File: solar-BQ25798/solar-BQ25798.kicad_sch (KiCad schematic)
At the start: 72 parts, among them J101 Power In, J102 Power OUT, J103 Power OUT

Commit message: BQ25798 WIP
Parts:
- removed BAT_N116: MY-18650-05-J, cacophony-library:BAT-TH_MY-18650-05-J, symbol cacophony-library:MY-18650-05-J
- removed BAT_P116: MY-18650-04-J, cacophony-library:BAT-TH_MY-18650-04-J, symbol cacophony-library:MY-18650-04-J
- added D101: D_Zener, Diode_SMD:D_SOD-123, symbol Device:D_Zener
- added Q101: DMP4013LFGQ-13, Package_SON:Diodes_PowerDI3333-8, symbol cacophony-library:DMP4013LFGQ-13
- added R102: 100k, Resistor_SMD:R_0402_1005Metric, symbol Device:R
- F101, F102: value Fuse -> 8A; footprint Fuse:Fuse_0805_2012Metric -> Fuse:Fuse_1206_3216Metric; LCSC Part (none) -> C187562
- R101: value 1k -> 10k; footprint Resistor_SMD:R_0603_1608Metric -> Resistor_SMD:R_0402_1005Metric; LCSC Part (none) -> C25744
- renumbered FL102 to FL101, FL103 to FL102, H105 to H102, H109 to H103, H102 to H104, H106 to H105, H110 to H106, H103 to H107, H107 to H108, H111 to H109, H104 to H110, H108 to H111, H117 to H114, H121 to H115, H114 to H116, H118 to H117, H122 to H118, H115 to H119, H119 to H120, H123 to H121, H116 to H122, H120 to H123, H129 to H126, H126 to H127, H130 to H128, H127 to H129, H131 to H130, H128 to H131, J103 to J102, J102 to J103
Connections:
- net GND: now also R102.1; no longer FL102.2
- net GND_OUT_FILTERED: now also J102.2 (Pin_2), J103.2 (Pin_2); no longer J102.1 (Pin_1), J103.1 (Pin_1)
- net POWER_IN_FILTERED: now also FL101.3, Q101.5 (D); no longer F101.2, FL101.2
- net V_BATT_FUSED: now also J102.1 (Pin_1), J103.1 (Pin_1); no longer J102.2 (Pin_2), J103.2 (Pin_2)
- net V_{IN}: now also D101.1 (K), Q101.1 (S), Q101.2 (S), Q101.3 (S); no longer FL101.3
- net GND_IN_FILTERED renamed GND_IN_PHY
- net V_BATT renamed PACK_+
- net cell_S1_1/BAT+ renamed cell_S1_1/CELL+
- net cell_S1_1/BAT- renamed cell_S1_1/CELL-
- net cell_10/BAT+ renamed cell_S1_10/CELL+
- net cell_10/BAT- renamed cell_S1_10/CELL-
- net cell_11/BAT+ renamed cell_S1_11/CELL+
- net cell_11/BAT- renamed cell_S1_11/CELL-
- net cell_12/BAT+ renamed cell_S1_12/CELL+
- net cell_12/BAT- renamed cell_S1_12/CELL-
- net cell_13/BAT+ renamed cell_S1_13/CELL+
- net cell_13/BAT- renamed cell_S1_13/CELL-
- net cell_14/BAT+ renamed cell_S1_14/CELL+
- net cell_14/BAT- renamed cell_S1_14/CELL-
- net cell_15/BAT+ renamed cell_S1_15/CELL+
- net cell_15/BAT- renamed cell_S1_15/CELL-
- net cell_2/BAT+ renamed cell_S1_2/CELL+
- net cell_2/BAT- renamed cell_S1_2/CELL-
- net cell_3/BAT+ renamed cell_S1_3/CELL+
- net cell_3/BAT- renamed cell_S1_3/CELL-
- net cell_4/BAT+ renamed cell_S1_4/CELL+
- net cell_4/BAT- renamed cell_S1_4/CELL-
- net cell_5/BAT+ renamed cell_S1_5/CELL+
- net cell_5/BAT- renamed cell_S1_5/CELL-
- net cell_6/BAT+ renamed cell_S1_6/CELL+
- net cell_6/BAT- renamed cell_S1_6/CELL-
- net cell_7/BAT+ renamed cell_S1_7/CELL+
- net cell_7/BAT- renamed cell_S1_7/CELL-
- net cell_8/BAT+ renamed cell_S1_8/CELL+
- net cell_8/BAT- renamed cell_S1_8/CELL-
- net cell_9/BAT+ renamed cell_S1_9/CELL+
- net cell_9/BAT- renamed cell_S1_9/CELL-
- new net: D101.2 (A), Q101.4 (G), R102.2
- new net PACK_-: FL102.2
- new net POWER_IN_FUSED: F101.2, FL101.2
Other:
- sheet cell_1 renamed cell_S1_1
- removed sheet LTC4015 Sheet
- removed sheet cell_10
- removed sheet cell_11
- removed sheet cell_12
- removed sheet cell_13
- removed sheet cell_14
- removed sheet cell_15
- removed sheet cell_16
- removed sheet cell_2
- removed sheet cell_3
- removed sheet cell_4
- removed sheet cell_5
- removed sheet cell_6
- removed sheet cell_7
- removed sheet cell_8
- removed sheet cell_9
- added sheet ATtiny1616 (attiny1616.kicad_sch)
- added sheet BQ25798 (BQ25798.kicad_sch)
- added sheet BQ76920 (bq76920.kicad_sch)
- added sheet cell_S1_10 (cell_S1_1.kicad_sch)
- added sheet cell_S1_11 (cell_S1_1.kicad_sch)
- added sheet cell_S1_12 (cell_S1_1.kicad_sch)
- added sheet cell_S1_13 (cell_S1_1.kicad_sch)
- added sheet cell_S1_14 (cell_S1_1.kicad_sch)
- added sheet cell_S1_15 (cell_S1_1.kicad_sch)
- added sheet cell_S1_2 (cell_S1_1.kicad_sch)
- added sheet cell_S1_3 (cell_S1_1.kicad_sch)
- added sheet cell_S1_4 (cell_S1_1.kicad_sch)
- added sheet cell_S1_5 (cell_S1_1.kicad_sch)
- added sheet cell_S1_6 (cell_S1_1.kicad_sch)
- added sheet cell_S1_7 (cell_S1_1.kicad_sch)
- added sheet cell_S1_8 (cell_S1_1.kicad_sch)
- added sheet cell_S1_9 (cell_S1_1.kicad_sch)
- sheet cell_S1_1: file cell_1.kicad_sch -> cell_S1_1.kicad_sch
- sheet cell_S1_1 ports: added CELL+, CELL-, CELL_PROTECTED+, CELL_PROTECTED-; removed BAT+, BAT-
- moved on the sheet: BAT_N101, BAT_P101, F101, F102, FL101, FL102, H101, H102, H103, H104, H105, H106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

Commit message: BQ25798 WIP
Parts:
- F101, F102: value 8A -> 4A; footprint Fuse:Fuse_1206_3216Metric -> cacophony-library:FUSE-SMD_2410F4A250V; LCSC Part C187562 -> C5220740
- renumbered BAT_N106 to BAT_N102, BAT_N111 to BAT_N103, BAT_N102 to BAT_N104, BAT_N107 to BAT_N105, BAT_N112 to BAT_N106, BAT_N103 to BAT_N107, BAT_N113 to BAT_N109, BAT_N104 to BAT_N110, BAT_N109 to BAT_N111, BAT_N114 to BAT_N112, BAT_N105 to BAT_N113, BAT_N110 to BAT_N114, BAT_P106 to BAT_P102, BAT_P111 to BAT_P103, BAT_P102 to BAT_P104, BAT_P107 to BAT_P105, BAT_P112 to BAT_P106, BAT_P103 to BAT_P107, BAT_P113 to BAT_P109, BAT_P104 to BAT_P110, BAT_P109 to BAT_P111, BAT_P114 to BAT_P112, BAT_P105 to BAT_P113, BAT_P110 to BAT_P114, H104 to H102, H107 to H103, H110 to H104, H113 to H105, H116 to H106, H119 to H107, H122 to H108, H125 to H109, H127 to H110, H129 to H111, H131 to H112, H102 to H113, H105 to H114, H108 to H115, H111 to H116, H114 to H117, H117 to H118, H120 to H119, H123 to H120, H126 to H121, H128 to H122, H130 to H123, H132 to H124, H103 to H125, H106 to H126, H109 to H127, H112 to H128, H115 to H129, H118 to H130, H121 to H131, H124 to H132
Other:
- sheet cell_S1_1 renamed cell_01
- sheet cell_S1_10 renamed cell_10
- sheet cell_S1_11 renamed cell_11
- sheet cell_S1_12 renamed cell_12
- sheet cell_S1_13 renamed cell_13
- sheet cell_S1_14 renamed cell_14
- sheet cell_S1_15 renamed cell_15
- sheet cell_S1_2 renamed cell_02
- sheet cell_S1_3 renamed cell_03
- sheet cell_S1_4 renamed cell_04
- sheet cell_S1_5 renamed cell_05
- sheet cell_S1_6 renamed cell_06
- sheet cell_S1_7 renamed cell_07
- sheet cell_S1_8 renamed cell_08
- sheet cell_S1_9 renamed cell_09
- sheet BQ76920: file bq76920.kicad_sch -> BQ76920.kicad_sch
- sheet cell_01: file cell_S1_1.kicad_sch -> cell.kicad_sch
- sheet cell_02: file cell_S1_1.kicad_sch -> cell.kicad_sch
- sheet cell_03: file cell_S1_1.kicad_sch -> cell.kicad_sch
- sheet cell_04: file cell_S1_1.kicad_sch -> cell.kicad_sch
- sheet cell_05: file cell_S1_1.kicad_sch -> cell.kicad_sch
- sheet cell_06: file cell_S1_1.kicad_sch -> cell.kicad_sch
- sheet cell_07: file cell_S1_1.kicad_sch -> cell.kicad_sch
- sheet cell_08: file cell_S1_1.kicad_sch -> cell.kicad_sch
- sheet cell_09: file cell_S1_1.kicad_sch -> cell.kicad_sch
- sheet cell_10: file cell_S1_1.kicad_sch -> cell.kicad_sch
- sheet cell_11: file cell_S1_1.kicad_sch -> cell.kicad_sch
- sheet cell_12: file cell_S1_1.kicad_sch -> cell.kicad_sch
- sheet cell_13: file cell_S1_1.kicad_sch -> cell.kicad_sch
- sheet cell_14: file cell_S1_1.kicad_sch -> cell.kicad_sch
- sheet cell_15: file cell_S1_1.kicad_sch -> cell.kicad_sch
- note removed: "C2915633"
- moved on the sheet: BAT_N101, BAT_N102, BAT_N103, BAT_N104, BAT_N105, BAT_N106, BAT_N107, BAT_N108, BAT_N109, BAT_N110, BAT_N111, BAT_N112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

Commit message: Solar battery WIP
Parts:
- added C101, C102: 1uF, Capacitor_SMD:C_0603_1608Metric, symbol Device:C_Small
- added D102, D103: D, Diode_SMD:D_SOD-323_HandSoldering, symbol Device:D
- added JP101: Jumper_2_Open, Connector_PinHeader_2.00mm:PinHeader_2x01_P2.00mm_Vertical, symbol Jumper:Jumper_2_Open
- added JP102: SolderJumper_2_Bridged, cacophony-library:SolderJumper-2_P1.3mm_Bridged_RoundedPad1.0x1.5mm, symbol Jumper:SolderJumper_2_Bridged
- added Q102: 2N7002, Package_TO_SOT_SMD:SOT-23, symbol Transistor_FET:2N7002
- added R103: 30k, Resistor_SMD:R_0402_1005Metric, symbol Device:R
- added R104: 10k, Resistor_SMD:R_0402_1005Metric, symbol Device:R
- added U101: HT75xx-1-SOT89, Package_TO_SOT_SMD:SOT-89-3, symbol Regulator_Linear:HT75xx-1-SOT89
- BAT_N101, BAT_N108, BAT_N115: footprint cacophony-library:BAT-TH_MY-18650-05-J -> cacophony-library:BAT-TH_MY-18650-05-J-2
- BAT_N102: renamed from BAT_N104; footprint cacophony-library:BAT-TH_MY-18650-05-J -> cacophony-library:BAT-TH_MY-18650-05-J-2
- BAT_N103: renamed from BAT_N107; footprint cacophony-library:BAT-TH_MY-18650-05-J -> cacophony-library:BAT-TH_MY-18650-05-J-2
- BAT_N104: renamed from BAT_N110; footprint cacophony-library:BAT-TH_MY-18650-05-J -> cacophony-library:BAT-TH_MY-18650-05-J-2
- BAT_N105: renamed from BAT_N113; footprint cacophony-library:BAT-TH_MY-18650-05-J -> cacophony-library:BAT-TH_MY-18650-05-J-2
- BAT_N106: renamed from BAT_N102; footprint cacophony-library:BAT-TH_MY-18650-05-J -> cacophony-library:BAT-TH_MY-18650-05-J-2
- BAT_N107: renamed from BAT_N105; footprint cacophony-library:BAT-TH_MY-18650-05-J -> cacophony-library:BAT-TH_MY-18650-05-J-2
- BAT_N109: renamed from BAT_N111; footprint cacophony-library:BAT-TH_MY-18650-05-J -> cacophony-library:BAT-TH_MY-18650-05-J-2
- BAT_N110: renamed from BAT_N114; footprint cacophony-library:BAT-TH_MY-18650-05-J -> cacophony-library:BAT-TH_MY-18650-05-J-2
- BAT_N111: renamed from BAT_N103; footprint cacophony-library:BAT-TH_MY-18650-05-J -> cacophony-library:BAT-TH_MY-18650-05-J-2
- BAT_N112: renamed from BAT_N106; footprint cacophony-library:BAT-TH_MY-18650-05-J -> cacophony-library:BAT-TH_MY-18650-05-J-2
- BAT_N113: renamed from BAT_N109; footprint cacophony-library:BAT-TH_MY-18650-05-J -> cacophony-library:BAT-TH_MY-18650-05-J-2
- BAT_N114: renamed from BAT_N112; footprint cacophony-library:BAT-TH_MY-18650-05-J -> cacophony-library:BAT-TH_MY-18650-05-J-2
- BAT_P101, BAT_P108, BAT_P115: footprint cacophony-library:BAT-TH_MY-18650-04-J -> cacophony-library:BAT-TH_MY-18650-test8_4.0_2.5
- BAT_P102: renamed from BAT_P104; footprint cacophony-library:BAT-TH_MY-18650-04-J -> cacophony-library:BAT-TH_MY-18650-test8_4.0_2.5
- BAT_P103: renamed from BAT_P107; footprint cacophony-library:BAT-TH_MY-18650-04-J -> cacophony-library:BAT-TH_MY-18650-test8_4.0_2.5
- BAT_P104: renamed from BAT_P110; footprint cacophony-library:BAT-TH_MY-18650-04-J -> cacophony-library:BAT-TH_MY-18650-test8_4.0_2.5
- BAT_P105: renamed from BAT_P113; footprint cacophony-library:BAT-TH_MY-18650-04-J -> cacophony-library:BAT-TH_MY-18650-test8_4.0_2.5
- BAT_P106: renamed from BAT_P102; footprint cacophony-library:BAT-TH_MY-18650-04-J -> cacophony-library:BAT-TH_MY-18650-test8_4.0_2.5
- BAT_P107: renamed from BAT_P105; footprint cacophony-library:BAT-TH_MY-18650-04-J -> cacophony-library:BAT-TH_MY-18650-test8_4.0_2.5
- BAT_P109: renamed from BAT_P111; footprint cacophony-library:BAT-TH_MY-18650-04-J -> cacophony-library:BAT-TH_MY-18650-test8_4.0_2.5
- BAT_P110: renamed from BAT_P114; footprint cacophony-library:BAT-TH_MY-18650-04-J -> cacophony-library:BAT-TH_MY-18650-test8_4.0_2.5
- BAT_P111: renamed from BAT_P103; footprint cacophony-library:BAT-TH_MY-18650-04-J -> cacophony-library:BAT-TH_MY-18650-test8_4.0_2.5
- BAT_P112: renamed from BAT_P106; footprint cacophony-library:BAT-TH_MY-18650-04-J -> cacophony-library:BAT-TH_MY-18650-test8_4.0_2.5
- BAT_P113: renamed from BAT_P109; footprint cacophony-library:BAT-TH_MY-18650-04-J -> cacophony-library:BAT-TH_MY-18650-test8_4.0_2.5
- BAT_P114: renamed from BAT_P112; footprint cacophony-library:BAT-TH_MY-18650-04-J -> cacophony-library:BAT-TH_MY-18650-test8_4.0_2.5
- renumbered F102 to F101, F101 to F102, FL102 to FL101, FL101 to FL102, H113 to H102, H125 to H103, H109 to H104, H102 to H105, H114 to H106, H126 to H107, H110 to H108, H103 to H109, H115 to H110, H127 to H111, H111 to H112, H104 to H113, H116 to H114, H128 to H115, H121 to H116, H105 to H117, H117 to H118, H129 to H119, H122 to H120, H106 to H121, H118 to H122, H130 to H123, H123 to H124, H107 to H125, H119 to H126, H131 to H127, H112 to H128, H108 to H129, H120 to H130, H132 to H131, H124 to H132, J103 to J101, J101 to J102, J102 to J103
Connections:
- net GND: now also FL102.3, C101.1, C102.1, Q102.2 (S), R104.2, U101.1 (GND); no longer FL102.4
- net GND_IN_PHY: now also FL102.2; no longer FL102.1
- net PACK_+: now also D102.2 (A), JP101.2 (B), JP102.2 (B)
- net POWER_IN_FILTERED: now also FL102.4; no longer FL102.3
- net POWER_IN_FUSED: now also FL102.1; no longer FL102.2
- net V_{IN}: now also D103.2 (A)
- net V_{SENSE}: now also Q102.3 (D), R103.1
- new net +3.3V: C102.2, U101.3 (VOUT)
- new net PACK_+_PHY: JP101.1 (A), JP102.1 (A)
- new net PRE_LIN_REG: C101.2, D102.1 (K), D103.1 (K), U101.2 (VIN)
- new net PULL_SENSE_LOW: Q102.1 (G)
- new net SENSE_DIV: R103.2, R104.1
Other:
- note added: "3.3V Power supply"
- note added: "Mounting Holes"
- note added: "Power In"
- note added: "Power OUT"
- moved on the sheet: BAT_N101, BAT_N102, BAT_N103, BAT_N104, BAT_N105, BAT_N106, BAT_N107, BAT_N108, BAT_N109, BAT_N110, BAT_N111, BAT_N112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

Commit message: Version v0.0.2
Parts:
- JP101: now left out of the parts list
- Q102: LCSC Part (none) -> C8545
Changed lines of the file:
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@@
 		(unit 1)
 		(exclude_from_sim no)
-		(in_bom yes)
+		(in_bom no)
 		(on_board yes)
 		(dnp no)
@@
 			(at 144.78 55.88 0)
 			(effects
+				(font
+					(size 1.27 1.27)
+				)
+				(hide yes)
+			)
+		)
+		(property "LCSC Part" "C8545"
+			(at 144.78 55.88 0)
+			(effects

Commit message: Tidy up of files
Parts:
- added C?: 22pF, Capacitor_SMD:C_0402_1005Metric, symbol Device:C_Small
- added Q103: 2N7002, Package_TO_SOT_SMD:SOT-23, symbol Transistor_FET:2N7002
- added R105, R107, R?: 10k, Resistor_SMD:R_0402_1005Metric, symbol Device:R
- added R106: 30k, Resistor_SMD:R_0402_1005Metric, symbol Device:R
- added R108, R?: 1M, Resistor_SMD:R_0603_1608Metric, symbol Device:R
- added R?: 470k, Resistor_SMD:R_0402_1005Metric, symbol Device:R
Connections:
- net GND: now also C?.1, Q103.2 (S), R107.2, R?.2
- net PULL_SENSE_LOW: now also Q103.1 (G)
- net SENSE_DIV: now also R106.2, R107.1
- new net: Q103.3 (D), R105.1, R106.1, R108.1
- new net +12V: R105.2
- new net BATTERY_LV: R108.2, R?.1
- new net BATT_SENSE_LV: C?.2, R?.1, R?.2, R?.2
- new net BATT_SENSE_LV_PHY: R?.1

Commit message: Update battery PCB
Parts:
- removed C?: 22pF, Capacitor_SMD:C_0402_1005Metric, symbol Device:C_Small
- removed H109, H113: MountingHole, cacophony-library:MountingHole_3.2mm_no_bolt_head, symbol Mechanical:MountingHole
- removed JP101: Jumper_2_Open, Connector_PinHeader_2.00mm:PinHeader_2x01_P2.00mm_Vertical, symbol Jumper:Jumper_2_Open
- removed JP102: SolderJumper_2_Bridged, cacophony-library:SolderJumper-2_P1.3mm_Bridged_RoundedPad1.0x1.5mm, symbol Jumper:SolderJumper_2_Bridged
- removed Q103: 2N7002, Package_TO_SOT_SMD:SOT-23, symbol Transistor_FET:2N7002
- removed R105, R107, R?: 10k, Resistor_SMD:R_0402_1005Metric, symbol Device:R
- removed R106: 30k, Resistor_SMD:R_0402_1005Metric, symbol Device:R
- removed R108, R?: 1M, Resistor_SMD:R_0603_1608Metric, symbol Device:R
- removed R?: 470k, Resistor_SMD:R_0402_1005Metric, symbol Device:R
- added C103: 100n, Capacitor_SMD:C_0402_1005Metric, symbol Device:C_Small
- added R107: 0Ω, cacophony-library:R_1206_Shunt, symbol Device:R_Shunt
- added U102: INA219AxDCN, Package_TO_SOT_SMD:SOT-23-8, symbol Sensor_Energy:INA219AxDCN
- BAT_N101, BAT_N108, BAT_N115: footprint cacophony-library:BAT-TH_MY-18650-05-J-2 -> cacophony-library:BAT-TH-18650-N
- BAT_N102: renamed from BAT_N106; footprint cacophony-library:BAT-TH_MY-18650-05-J-2 -> cacophony-library:BAT-TH-18650-N
- BAT_N103: renamed from BAT_N111; footprint cacophony-library:BAT-TH_MY-18650-05-J-2 -> cacophony-library:BAT-TH-18650-N
- BAT_N104: renamed from BAT_N102; footprint cacophony-library:BAT-TH_MY-18650-05-J-2 -> cacophony-library:BAT-TH-18650-N
- BAT_N105: renamed from BAT_N107; footprint cacophony-library:BAT-TH_MY-18650-05-J-2 -> cacophony-library:BAT-TH-18650-N
- BAT_N106: renamed from BAT_N112; footprint cacophony-library:BAT-TH_MY-18650-05-J-2 -> cacophony-library:BAT-TH-18650-N
- BAT_N107: renamed from BAT_N103; footprint cacophony-library:BAT-TH_MY-18650-05-J-2 -> cacophony-library:BAT-TH-18650-N
- BAT_N109: renamed from BAT_N113; footprint cacophony-library:BAT-TH_MY-18650-05-J-2 -> cacophony-library:BAT-TH-18650-N
- BAT_N110: renamed from BAT_N104; footprint cacophony-library:BAT-TH_MY-18650-05-J-2 -> cacophony-library:BAT-TH-18650-N
- BAT_N111: renamed from BAT_N109; footprint cacophony-library:BAT-TH_MY-18650-05-J-2 -> cacophony-library:BAT-TH-18650-N
- BAT_N112: renamed from BAT_N114; footprint cacophony-library:BAT-TH_MY-18650-05-J-2 -> cacophony-library:BAT-TH-18650-N
- BAT_N113: renamed from BAT_N105; footprint cacophony-library:BAT-TH_MY-18650-05-J-2 -> cacophony-library:BAT-TH-18650-N
- BAT_N114: renamed from BAT_N110; footprint cacophony-library:BAT-TH_MY-18650-05-J-2 -> cacophony-library:BAT-TH-18650-N
- BAT_P101, BAT_P108, BAT_P115: footprint cacophony-library:BAT-TH_MY-18650-test8_4.0_2.5 -> cacophony-library:BAT-TH-18650-P_silkscreen
- BAT_P102: renamed from BAT_P106; footprint cacophony-library:BAT-TH_MY-18650-test8_4.0_2.5 -> cacophony-library:BAT-TH-18650-P_silkscreen
- BAT_P103: renamed from BAT_P111; footprint cacophony-library:BAT-TH_MY-18650-test8_4.0_2.5 -> cacophony-library:BAT-TH-18650-P_silkscreen
- BAT_P104: renamed from BAT_P102; footprint cacophony-library:BAT-TH_MY-18650-test8_4.0_2.5 -> cacophony-library:BAT-TH-18650-P_silkscreen
- BAT_P105: renamed from BAT_P107; footprint cacophony-library:BAT-TH_MY-18650-test8_4.0_2.5 -> cacophony-library:BAT-TH-18650-P_silkscreen
- BAT_P106: renamed from BAT_P112; footprint cacophony-library:BAT-TH_MY-18650-test8_4.0_2.5 -> cacophony-library:BAT-TH-18650-P_silkscreen
- BAT_P107: renamed from BAT_P103; footprint cacophony-library:BAT-TH_MY-18650-test8_4.0_2.5 -> cacophony-library:BAT-TH-18650-P_silkscreen
- BAT_P109: renamed from BAT_P113; footprint cacophony-library:BAT-TH_MY-18650-test8_4.0_2.5 -> cacophony-library:BAT-TH-18650-P_silkscreen
- BAT_P110: renamed from BAT_P104; footprint cacophony-library:BAT-TH_MY-18650-test8_4.0_2.5 -> cacophony-library:BAT-TH-18650-P_silkscreen
- BAT_P111: renamed from BAT_P109; footprint cacophony-library:BAT-TH_MY-18650-test8_4.0_2.5 -> cacophony-library:BAT-TH-18650-P_silkscreen
- BAT_P112: renamed from BAT_P114; footprint cacophony-library:BAT-TH_MY-18650-test8_4.0_2.5 -> cacophony-library:BAT-TH-18650-P_silkscreen
- BAT_P113: renamed from BAT_P105; footprint cacophony-library:BAT-TH_MY-18650-test8_4.0_2.5 -> cacophony-library:BAT-TH-18650-P_silkscreen
- BAT_P114: renamed from BAT_P110; footprint cacophony-library:BAT-TH_MY-18650-test8_4.0_2.5 -> cacophony-library:BAT-TH-18650-P_silkscreen
- J102: renamed from J101; now not fitted; now left out of the parts list
- R103: value 30k -> 100k; LCSC Part C25553 -> C25741
- R104: value 10k -> 100k; LCSC Part C25744 -> C25741
- renumbered D102 to D101, D103 to D102, D101 to D103, F102 to F101, F101 to F102, FL102 to FL101, FL101 to FL102, H105 to H102, H117 to H105, H121 to H106, H125 to H107, H129 to H108, H102 to H109, H106 to H110, H110 to H111, H114 to H112, H118 to H113, H122 to H114, H126 to H115, H130 to H116, H103 to H117, H107 to H118, H111 to H119, H115 to H120, H119 to H121, H123 to H122, H127 to H123, H131 to H124, H104 to H125, H108 to H126, H112 to H127, H116 to H128, H120 to H129, H124 to H130, H128 to H131, J102 to J101, R102 to R101, R101 to R102
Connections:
- net +3.3V: now also C103.1, U102.4 (VS)
- net GND: now also FL101.4, R103.2, C103.2, U102.3 (GND); no longer FL101.3
- net GND_IN_PHY: now also FL101.1; no longer FL101.2
- net PACK_+: now also R107.4
- net PACK_+_PHY: now also R107.1
- net POWER_IN_FILTERED: now also FL101.3; no longer FL101.4
- net POWER_IN_FUSED: now also FL101.2; no longer FL101.1
- net V_{SENSE}: no longer R103.1
- net SENSE_DIV: no longer names the net of R104.1
- net SENSE_DIV: now also U102.7 (A0); no longer R103.2
- new net: R103.1, U102.8 (A1)
- new net: R107.2, U102.1 (IN+)
- new net: R107.3, U102.2 (IN-)
- new net SCL: U102.5 (SCL)
- new net SDA: U102.6 (SDA)

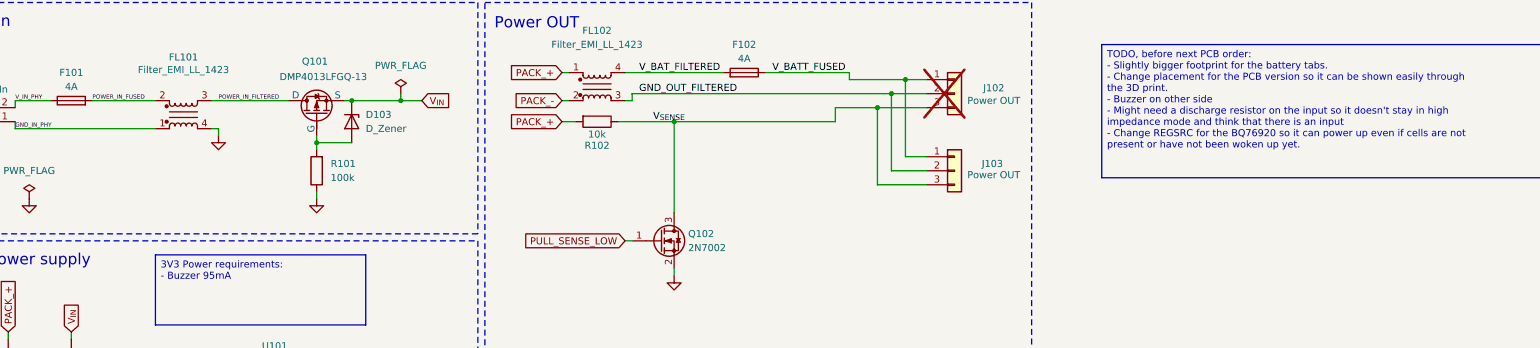
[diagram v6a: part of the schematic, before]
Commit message: Update to KiCAD 10
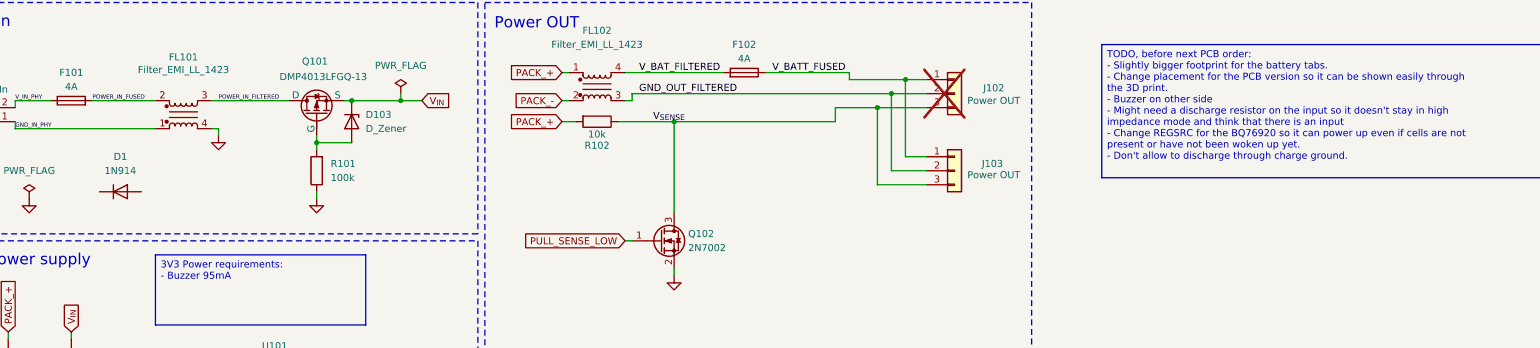
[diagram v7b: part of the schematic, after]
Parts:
- added D1: 1N914, Diode_THT:D_DO-35_SOD27_P7.62mm_Horizontal, symbol Diode:1N914
